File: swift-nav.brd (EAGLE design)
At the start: 52.5 x 49.8 mm, 164 parts, among them J1 SMA_EDGE, J6 ZX62-B-5PA, U1 6SLX9FTG256, U10 MAX2769, U12 PT7M8206B33TA5EX, U13 M25PX80, U2 LTC3407A_DFN, U3 STM32-M-64-LQFP, U4 7Q-16.368MBG-T, U5 SMA_PATCH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

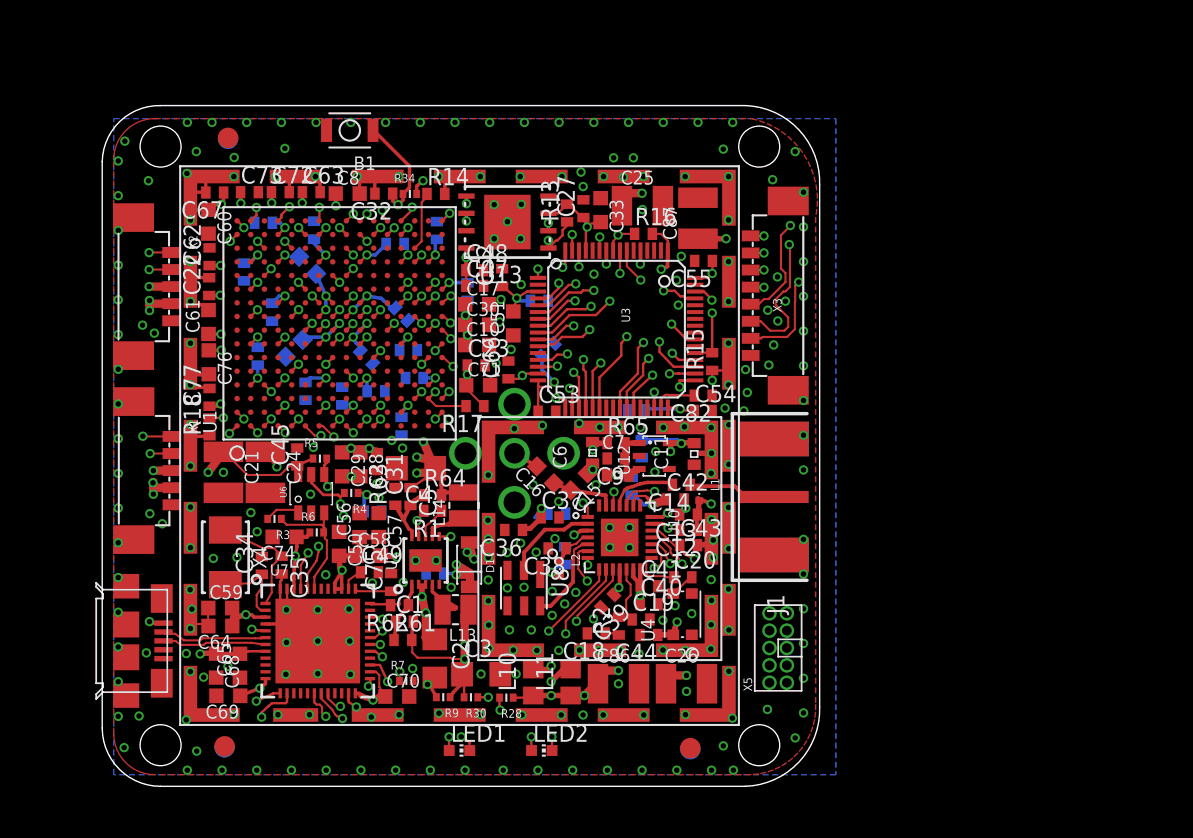
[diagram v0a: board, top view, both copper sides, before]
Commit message: Fixing DRC errors on board
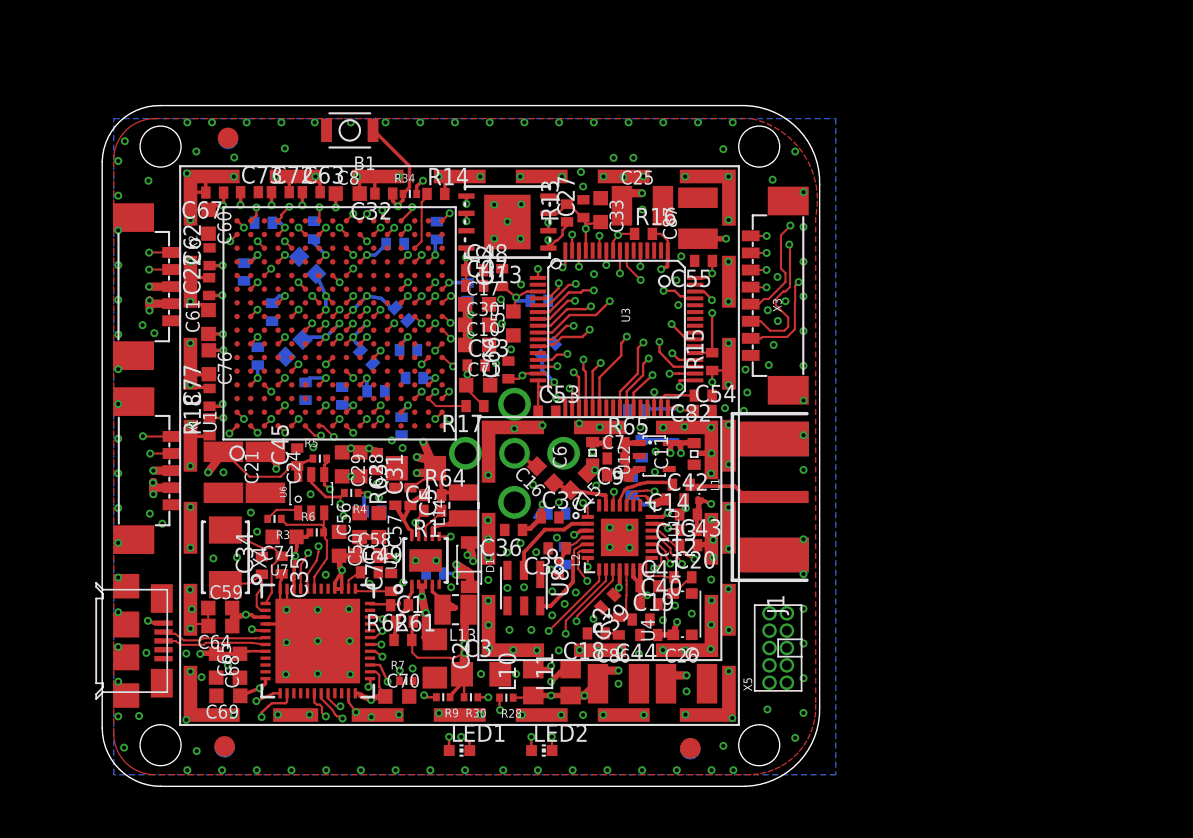
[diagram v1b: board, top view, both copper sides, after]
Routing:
- net VCC: track 34.4 -> 36.9 mm
- net VCCINT: track 59.3 -> 61.8 mm
- net VCCIO: track 184.8 -> 185.4 mm

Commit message: DRC complete
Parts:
- moved C88 0.46 mm to (26.1, 31.3)
- moved C94 0.26 mm to (36.9, 24.7)
- moved C46 0.14 mm to (18.9, 43.0)
- moved C45 0.13 mm to (18.0, 29.2)
- moved C93 0.13 mm to (37.6, 21.7)
- moved C103 0.10 mm to (25.1, 44.8)
- moved U6 0.10 mm to (19.0, 26.3)
- moved C89 0.10 mm to (21.2, 33.6)
- moved C104 0.10 mm to (15.6, 46.2)
- moved C14 0.09 mm to (46.0, 27.1)
- moved C21 0.08 mm to (12.6, 27.9)
- moved L13 0.08 mm to (29.6, 17.8)
- moved C100 0.06 mm to (19.2, 45.7)
- moved L1 0.06 mm to (47.5, 26.4)
- moved C102 0.05 mm to (15.1, 36.4)
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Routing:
- net FTDI_CLKOUT: track 23.7 -> 25.7 mm
- net GND: track 60.5 -> 61.9 mm
- net SPI2NSS_FLASH: track 87.4 -> 88.9 mm
- net SPI2SCK: track 126.2 -> 127.6 mm
- net VCCINT: track 61.8 -> 63.1 mm
- net SPI2MISO: track 35.6 -> 36.8 mm
- net N$19: track 2.43 -> 1.71 mm
- net DEBUG6: track 47.2 -> 46.5 mm
- net V+: track 111.4 -> 112.0 mm
- net N$21: track 42.4 -> 41.9 mm

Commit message: Corrected ground plane / traces under side mount SMA and straightened some traces
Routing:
- net JTAG_TMS: track 89.3 -> 208.2 mm, vias 3 -> 4
- net GND: track 61.9 -> 86.0 mm, vias 281 -> 282
- net UART1_TX: track 96.0 -> 100.6 mm, vias 2 -> 4
- net DEBUG5: track 50.6 -> 48.0 mm
- net VCCIO: track 185.5 -> 182.9 mm
- net UART1_RX: track 103.2 -> 105.6 mm, vias 3 -> 4
- net UART3_TX: track 123.0 -> 125.1 mm, vias 3 -> 4
- net UART3_RX: track 118.2 -> 120.2 mm, vias 3 -> 4
- net FTDI_CLKOUT: track 25.7 -> 24.2 mm
- net MAX_PGM: track 36.4 -> 35.2 mm
- net VCCINT: track 63.1 -> 62.3 mm
- net UART6_TX: track 85.5 -> 84.8 mm
- net JTAG_TDI: track 48.3 -> 48.8 mm, vias 1 -> 2
- net JTAG_TCK: track 100.6 -> 100.3 mm, vias 2 -> 3
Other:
- outline, holes or cut-outs redrawn

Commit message: Cleaned up routing somewhat, shortened trace lengths where easy to do so
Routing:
- net JTAG_TMS: track 208.2 -> 88.1 mm, vias 4 -> 3
- net SPI2SCK: track 127.6 -> 103.2 mm
- net JTAG_TCK: track 100.3 -> 76.7 mm
- net SPI2MOSI: track 127.7 -> 112.1 mm, vias 4 -> 6
- net SPI2NSS_FLASH: track 88.9 -> 77.5 mm
- net UART6_TX: track 84.8 -> 76.0 mm
- net VCCINT: track 62.3 -> 56.3 mm
- net JTAG_TDO: track 80.4 -> 75.0 mm, vias 4 -> 3
- net STM_TDO_FPGA_TDI: track 47.5 -> 42.4 mm
- net UART6_RX: track 89.5 -> 84.7 mm
- net MAX_PGM: track 35.2 -> 31.5 mm
- net N$21: track 41.9 -> 38.5 mm
- net SPI2NSS_FPGA: track 33.4 -> 29.9 mm
- net JTAG_TDI: track 48.8 -> 45.4 mm
- net N$29: track 32.7 -> 30.6 mm
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
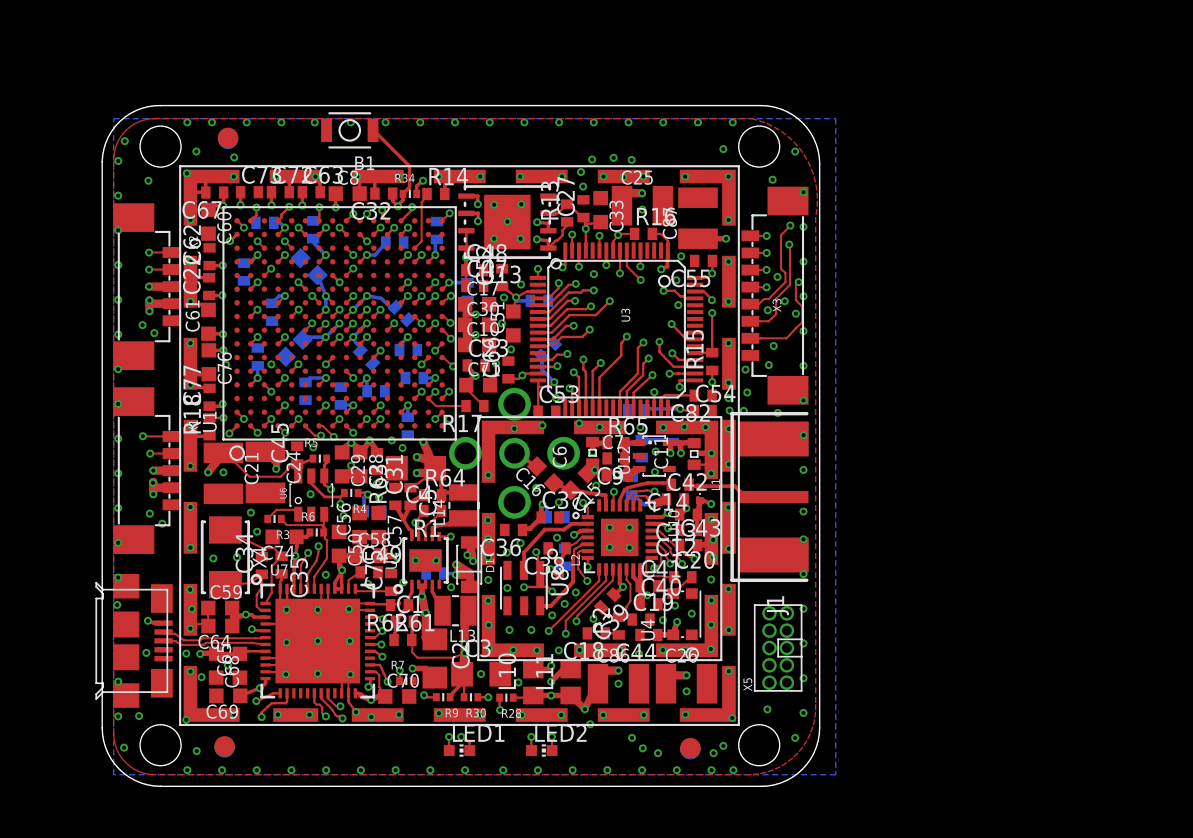
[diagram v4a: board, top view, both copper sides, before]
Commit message: Changed positions of picoblade headers and JTAG header, re-routing Rotated Spartan6 180 degrees
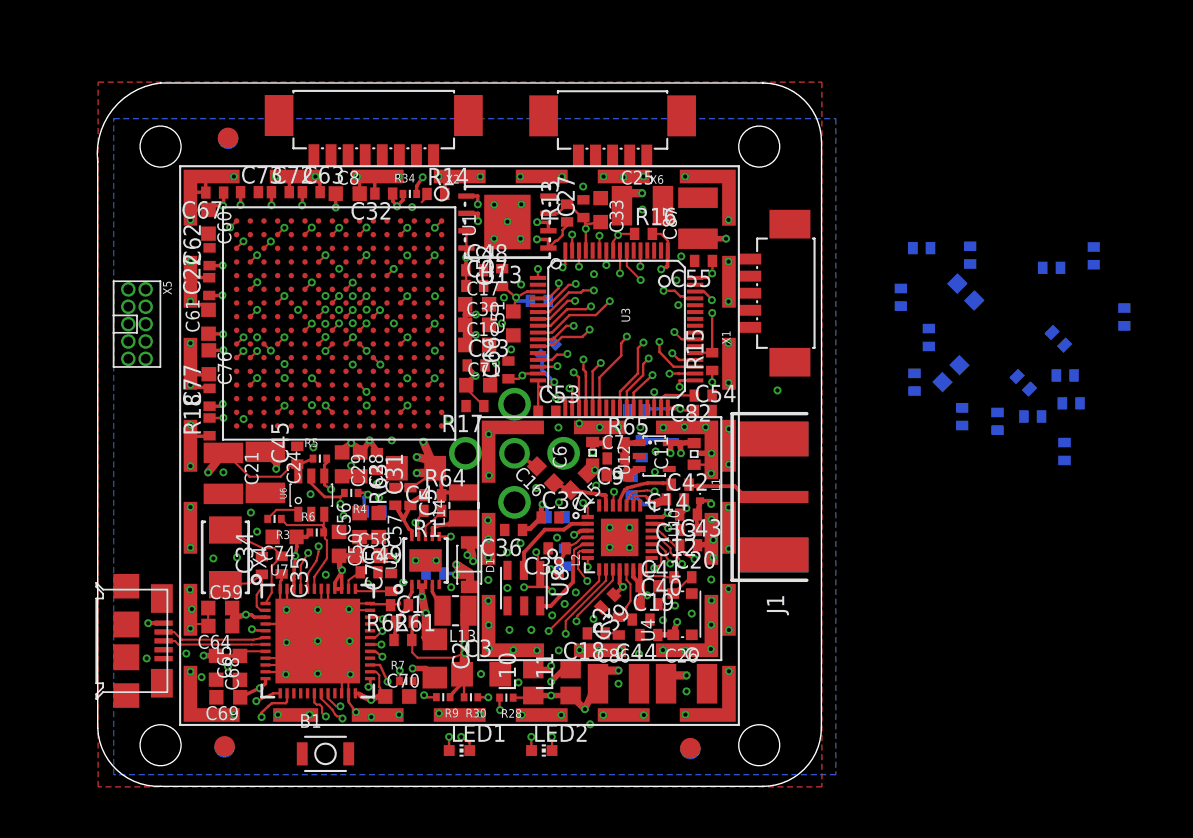
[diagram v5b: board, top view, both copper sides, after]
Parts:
- removed X3: (no value), pel_molex:PB-53398-08
- added X6: (no value), pel_molex:PB-53261-05
- X1: device pel_molex:PB-53398-05 -> pel_molex:PB-53261-05
- X2: device pel_molex:PB-53398-05 -> pel_molex:PB-53261-08
- moved X5 52.6 mm to (6.27, 38.8), turned to 270 degrees
- moved C100 48.1 mm to (67.2, 43.9)
- moved C80 48.1 mm to (71.1, 34.5)
- moved C95 48.1 mm to (71.8, 32.0)
- moved C99 48.1 mm to (74.2, 35.1)
- moved C81 48.1 mm to (78.5, 39.3)
- moved C88 48.1 mm to (74.1, 29.5)
- moved C101 48.1 mm to (62.2, 40.8)
- moved C102 48.1 mm to (63.2, 34.6)
- moved C103 48.1 mm to (73.2, 42.9)
- moved C104 48.1 mm to (63.7, 44.4)
- moved C105 48.1 mm to (64.2, 37.8)
- moved C106 48.1 mm to (66.7, 32.0)
- moved C46 48.1 mm to (66.9, 41.2)
- moved C78 48.1 mm to (73.7, 37.7)
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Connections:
- removed net STM_TDO_FPGA_TDI: U1.C12, U3.55
- new net FPGA_TDO_STM_TDI: U1.E14, U3.50
- net DEBUG0: now also X2.8; no longer X3.8
- net DEBUG1: now also X2.7; no longer X3.7
- net DEBUG2: now also X2.6; no longer X3.6
- net DEBUG3: now also X2.5; no longer X3.5
- net DEBUG4: now also X2.4; no longer X3.4
- net DEBUG5: now also X2.3; no longer X3.3
- net DEBUG6: now also X2.2; no longer X3.2
- net GND: now also X2.1, X6.5; no longer X2.5, X3.1
- net JTAG_TDI: now also U1.C12; no longer U3.50
- net JTAG_TDO: now also U3.55; no longer U1.E14
- net UART1_RX: now also X6.1; no longer X1.1
- net UART1_TX: now also X6.2; no longer X1.2
- net UART3_RX: now also X1.1; no longer X2.1
- net UART3_TX: now also X1.2; no longer X2.2
- net V+: now also X6.4; no longer X2.4
- net VCCIO: now also X6.3; no longer X2.3
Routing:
- net UART3_TX: track 124.8 -> 3.81 mm, vias 4 -> 1
- net UART3_RX: track 119.8 -> 1.87 mm, vias 4 -> 1
- net N$39: track 114.6 -> 6.16 mm, vias 3 -> 2
- net N$59: track 108.2 -> 2.08 mm, vias 3 -> 2
- net UART1_RX: track 104.6 -> 2.99 mm, vias 4 -> 1
- net UART1_TX: track 100.3 -> 4.27 mm, vias 4 -> 1
- net JTAG_TMS: track 88.1 -> 7.72 mm, vias 3 -> 1
- net JTAG_TCK: track 76.7 -> 1.62 mm, vias 3 -> 1
- net JTAG_TDO: track 75.0 -> 1.79 mm, vias 3 -> 1
- net JTAG_RST: track 72.3 -> 4.71 mm
- net SPI2MOSI: track 112.1 -> 53.3 mm, vias 6 -> 4
- net UART6_RX: track 84.7 -> 29.9 mm
- net SPI2SCK: track 103.2 -> 51.0 mm
- net DEBUG5: track 48.0 -> 0.00 mm, vias 2 -> 0
- net UART6_TX: track 76.0 -> 28.3 mm
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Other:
- board size 52.5 x 49.8 mm -> 53 x 51.5 mm

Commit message: Routing rearranged board, changed position of FT232
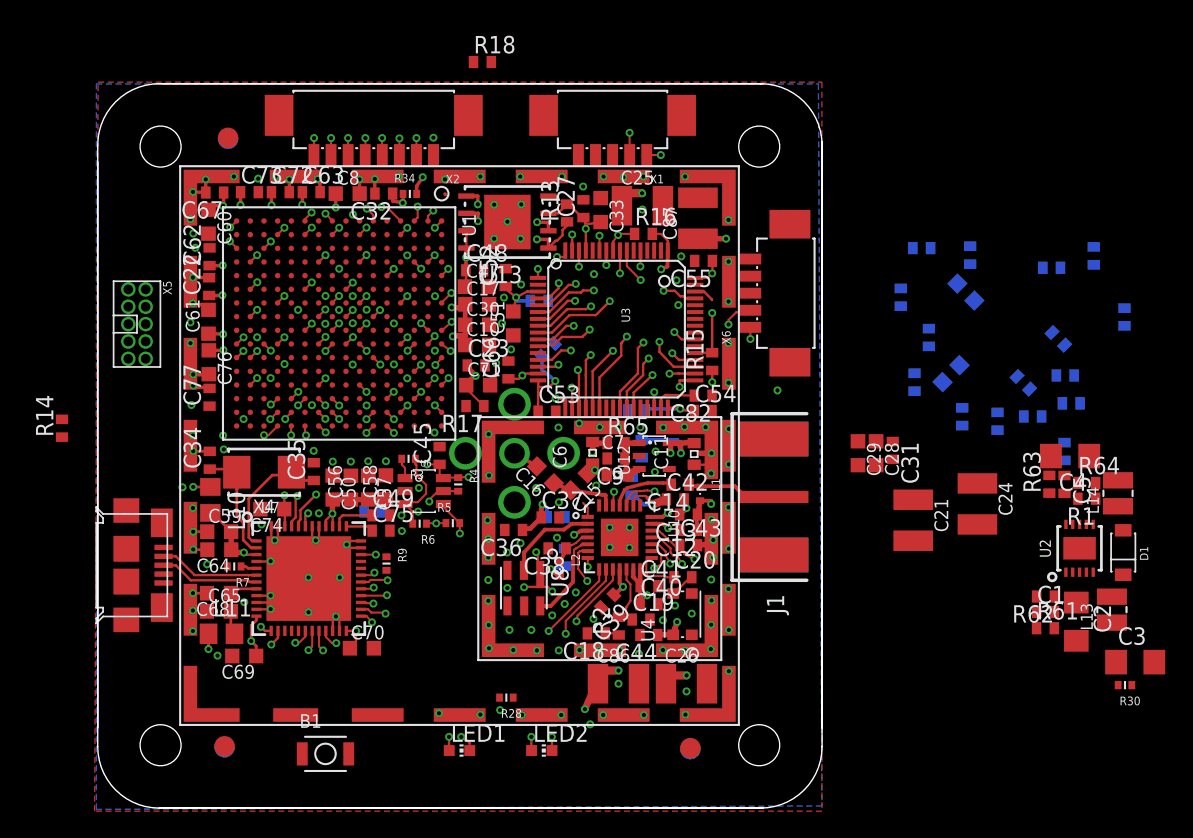
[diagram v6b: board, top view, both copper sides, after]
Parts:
- removed C96: 0.47uF, rcl:C0402
- C45, C56, C58, C64, C68, C69, C70, C74: value 47nF -> 0.047uF
- C47: device rcl:C0402 -> rcl:C0603K
- moved C24 52.1 mm to (67.8, 25.7)
- moved C21 50.6 mm to (63.1, 24.5)
- moved L13 48.0 mm to (77.6, 17.9), turned to 90 degrees
- moved U2 47.9 mm to (75.2, 22.4)
- moved C4 47.9 mm to (74.5, 29.2)
- moved C5 47.9 mm to (74.1, 27.1)
- moved R30 47.9 mm to (78.6, 12.4)
- moved R63 47.9 mm to (73.0, 27.1)
- moved R64 47.9 mm to (75.8, 27.2)
- moved C3 47.9 mm to (79.3, 14.1)
- moved D1 47.9 mm to (78.4, 22.1)
- moved L14 47.9 mm to (78.1, 26.4)
- moved R1 47.9 mm to (75.8, 26.0)
- moved R62 47.3 mm to (72.8, 18.9)
- moved R61 47.0 mm to (72.7, 16.6)
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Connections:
- new net FTDI_NOE: U1.K16, U7.30
- new net FTDI_NRD: U1.L14, U7.26
- new net FTDI_NRXF: U1.M15, U7.21
- new net FTDI_NSIWU: U1.K15, U7.28
- net DEBUG0: now also U1.L1; no longer U1.B16
- net DEBUG1: now also U1.J1; no longer U1.D16
- net DEBUG2: now also U1.G1; no longer U1.G16
- net DEBUG3: now also U1.F1; no longer U1.F15
- net DEBUG4: now also U1.D1; no longer U1.M16
- net DEBUG5: now also U1.C1; no longer U1.M15
- net DEBUG6: now also U1.B1; no longer U1.N16
- net FTDI_ADBUS5: now also U1.N14; no longer U1.A2
- net FTDI_ADBUS6: now also U1.N16; no longer U1.B1
- net FTDI_ADBUS7: now also U1.M14; no longer U1.C1
- net FTDI_CLKOUT: now also U1.K14; no longer U1.F1
- net FTDI_NTXE: now also U1.M16; no longer U1.D1
- net FTDI_NWR: now also U1.L16; no longer U1.E1
- net GND: no longer C96.2
- net MAX_CLKOUT: now also U1.J14; no longer U1.G1
- net MAX_I0: now also U1.E16; no longer U1.K1
- net MAX_I1: now also U1.E15; no longer U1.L1
- net MAX_Q0: now also U1.F15; no longer U1.J1
- net MAX_Q1: now also U1.F16; no longer U1.H1
- net SPI1MISO: now also U1.A13; no longer U1.T7
- net SPI1MOSI: now also U1.A11; no longer U1.T6
- net SPI1NSS: now also U1.A10; no longer U1.T9
- net SPI1SCK: now also U1.B10; no longer U1.T8
- net SPI2NSS_FPGA: no longer U1.J12
- net TIM2CH1ETR: now also U1.C10; no longer U1.J16
- net TIM2CH2: now also U1.A9; no longer U1.J14
- net TIM2CH3: now also U1.A7; no longer U1.K16
- net TIM2CH4: now also U1.A5; no longer U1.K15
- net V+: no longer C96.1
- net VCCIO: no longer U7.26, U7.30
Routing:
- net V+: track 65.3 -> 1.84 mm, vias 7 -> 1
- net JTAG_TCK: track 1.62 -> 50.9 mm, vias 1 -> 2
- net UART6_TX: track 28.3 -> 75.1 mm
- net JTAG_TDO: track 1.79 -> 47.2 mm, vias 1 -> 2
- net JTAG_TMS: track 7.72 -> 52.5 mm, vias 1 -> 2
- net V_USB: track 47.7 -> 3.02 mm, vias 4 -> 1
- net SPI2MOSI: track 53.3 -> 97.6 mm
- net UART6_RX: track 29.9 -> 72.5 mm
- net SPI2SCK: track 51.0 -> 88.5 mm
- net N$29: track 40.8 -> 5.54 mm, vias 2 -> 1
- net N$21: track 39.4 -> 5.06 mm, vias 2 -> 0
- net VCCIO: track 139.9 -> 113.7 mm, vias 64 -> 62
- net FTDI_NRD: track 0.00 -> 26.1 mm, vias 0 -> 2
- net FTDI_NRXF: track 0.00 -> 24.5 mm, vias 0 -> 2
- net FPGA_TDO_STM_TDI: track 1.91 -> 25.4 mm, vias 1 -> 2
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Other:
- board size 53 x 51.5 mm -> 53 x 53 mm

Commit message: All signals routed except caps on bottom layer
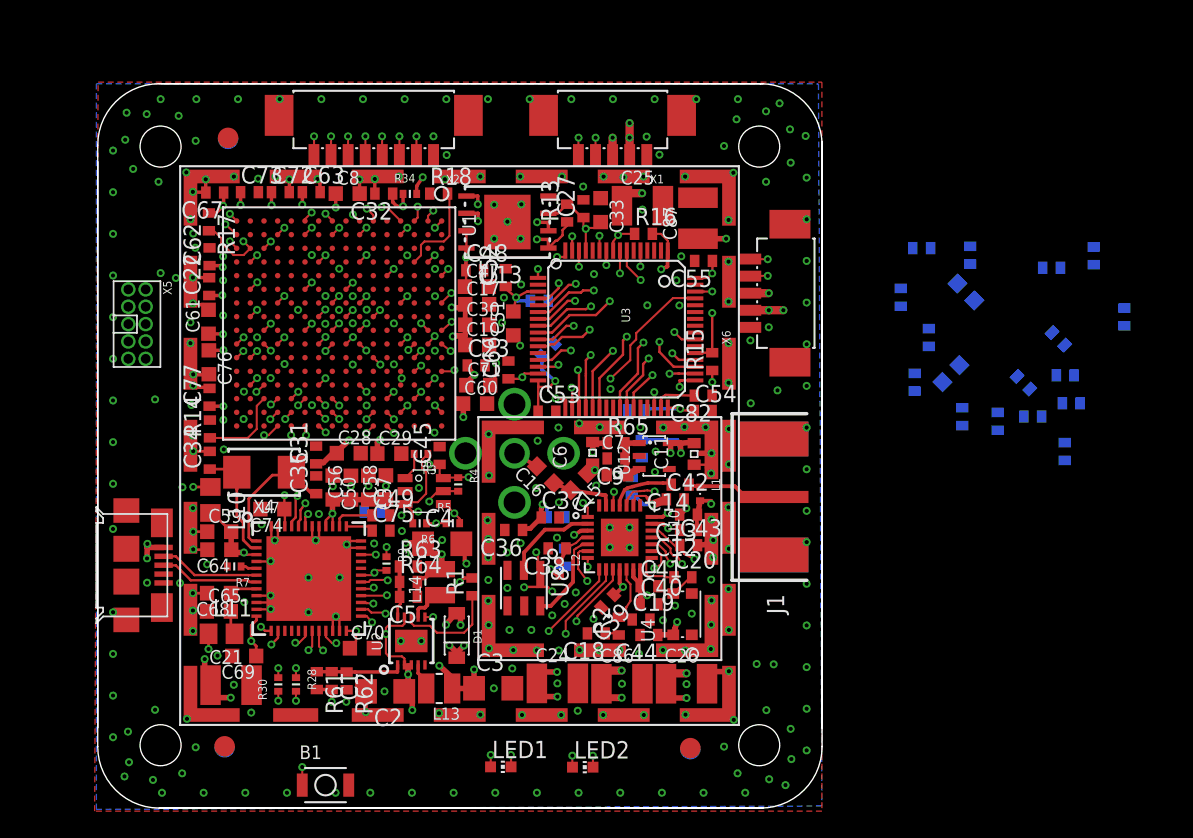
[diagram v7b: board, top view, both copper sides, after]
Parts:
- moved R30 62.0 mm to (16.6, 12.4), turned to 90 degrees
- moved R61 53.5 mm to (19.4, 12.7), turned to 270 degrees
- moved C1 52.5 mm to (20.5, 12.7), turned to 270 degrees
- moved R62 51.5 mm to (21.6, 12.7), turned to 270 degrees
- moved C21 51.3 mm to (13.2, 12.4), turned to 0 degrees
- moved C2 50.8 mm to (24.4, 11.9), turned to 180 degrees
- moved R64 50.2 mm to (26.1, 20.0)
- moved L14 50.0 mm to (28.4, 19.9)
- moved L13 49.6 mm to (28.4, 12.2), turned to 180 degrees
- moved U2 49.4 mm to (26.3, 15.6)
- moved D1 49.1 mm to (29.7, 16.0)
- moved C5 48.7 mm to (26.1, 18.9), turned to 180 degrees
- moved R63 47.3 mm to (26.1, 21.1), turned to 0 degrees
- moved C3 47.0 mm to (32.3, 12.2)
- moved C4 46.4 mm to (28.6, 22.7), turned to 0 degrees
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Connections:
- net GND: now also X1.1, X6.1; no longer X1.5, X6.5
- net SPI1MISO: now also U1.A12; no longer U1.A13
- net SPI1MOSI: now also U1.C11; no longer U1.A11
- net UART1_RX: now also X6.5; no longer X6.1
- net UART1_TX: now also X6.4; no longer X6.2
- net UART3_RX: now also X1.5; no longer X1.1
- net UART3_TX: now also X1.4; no longer X1.2
- net V+: now also X1.2, X6.2; no longer X1.4, X6.4
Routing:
- net V+: track 1.84 -> 136.0 mm, vias 1 -> 13
- net V_USB: track 3.02 -> 113.2 mm, vias 1 -> 5
- net FTDI_NRST: track 5.39 -> 113.1 mm
- net MAX_ANT_FLAG: track 7.37 -> 112.4 mm, vias 1 -> 3
- net JTAG_RST: track 4.53 -> 93.9 mm, vias 2 -> 4
- net MAX_NSHDN: track 2.17 -> 62.0 mm, vias 1 -> 2
- net VCCINT: track 12.6 -> 71.9 mm, vias 10 -> 16
- net N$39: track 6.16 -> 62.2 mm, vias 2 -> 3
- net N$59: track 2.08 -> 56.8 mm, vias 2 -> 3
- net MAX_LD: track 8.50 -> 58.8 mm
- net FPGA_PROGRAM_B: track 4.16 -> 52.4 mm, vias 1 -> 2
- net FPGA_DONE: track 2.50 -> 46.5 mm, vias 1 -> 2
- net FPGA_INIT_B: track 1.67 -> 38.3 mm, vias 1 -> 2
- net STM_CLK_IN: track 1.17 -> 37.2 mm, vias 1 -> 2
- net VCCIO: track 113.7 -> 142.9 mm, vias 62 -> 75
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- added copper zone on layer 15, net GND
